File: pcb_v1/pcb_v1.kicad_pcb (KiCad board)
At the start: 2 copper layers, 8 parts, among them IC1 ESP32-WROOM-32UE-H4, IC2 DWM3000TR13, IC3 TC1017-3.3VLTTR, J1 Conn_02x03_Counter_Clockwise

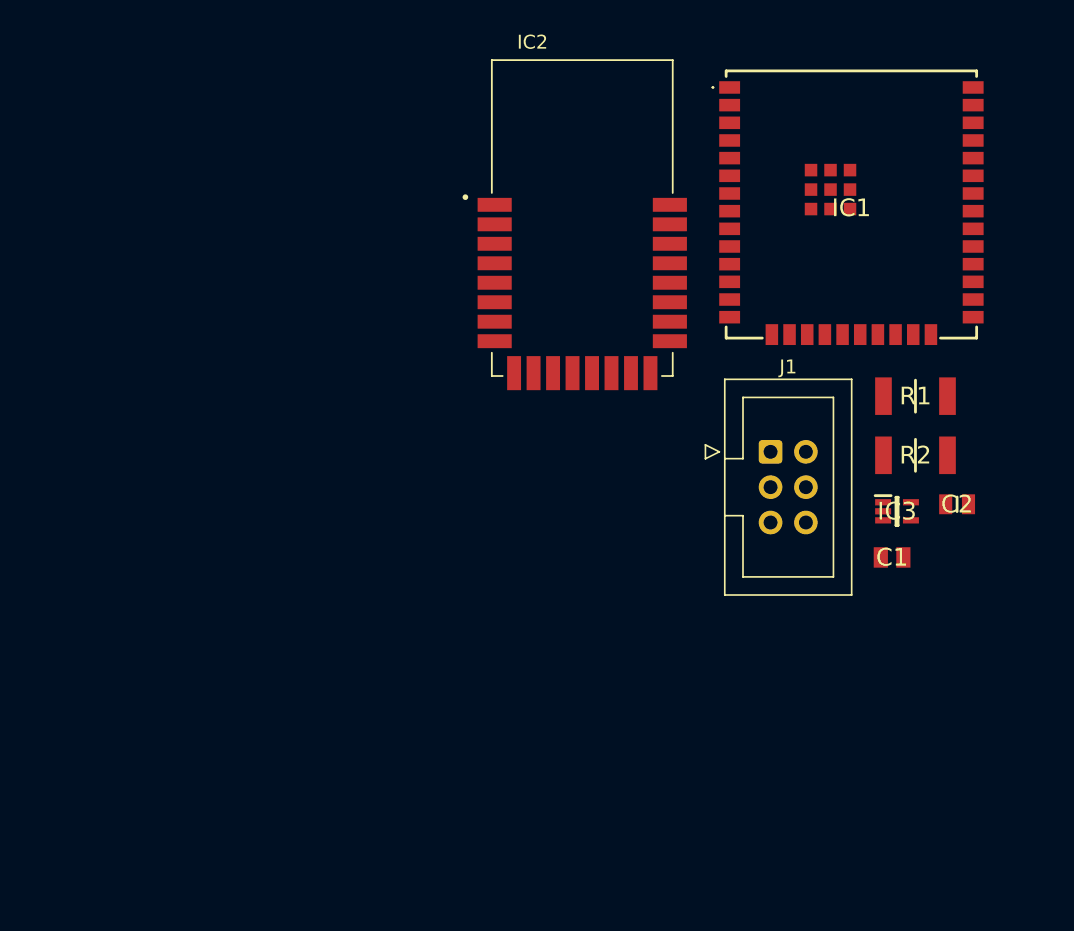
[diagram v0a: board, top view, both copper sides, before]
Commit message: pcb edits. add led footprints
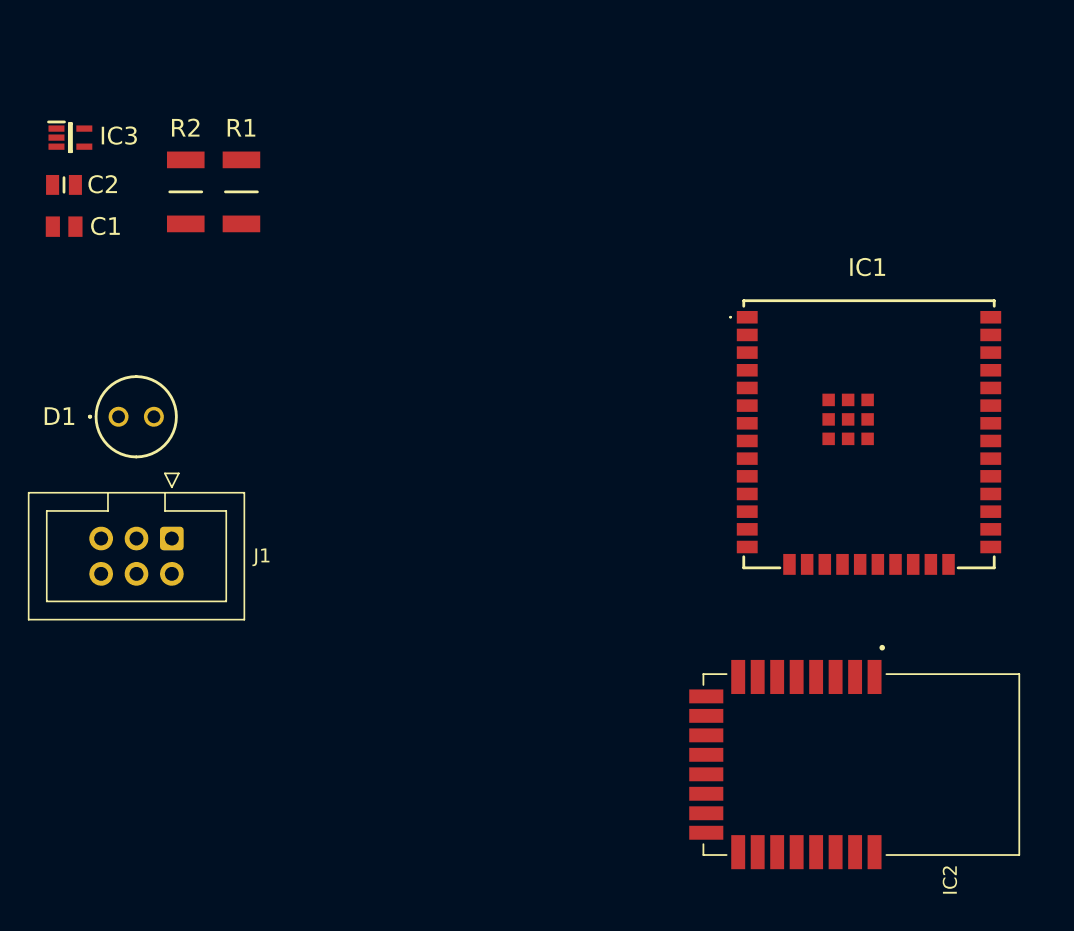
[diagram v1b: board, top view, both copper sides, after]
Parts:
- added D1: LED, led_footprint:QED123A4R0, F.Cu at (94.4, 99.0)
- moved C2 68.2 mm to (90.5, 82.3)
- moved IC3 65.2 mm to (91.0, 78.9)
- moved C1 64.1 mm to (90.5, 85.3), turned to 180 degrees
- moved R2 55.8 mm to (99.2, 82.8), turned to 90 degrees
- moved R1 50.6 mm to (103.2, 82.8), turned to 90 degrees
- moved IC2 44.1 mm to (147.8, 124.0), turned to -90 degrees
- moved J1 43.5 mm to (98.2, 107.7), turned to -90 degrees
- moved IC1 16.6 mm to (148.3, 100.2)

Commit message: update pin for jake baby
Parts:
- moved IC2 38.5 mm to (127.5, 91.2), turned to 0 degrees
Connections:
- IC2 pad 18: Net-(IC1-IO35) -> Net-(IC1-IO32)
- IC2 pad 19: Net-(IC1-IO32) -> Net-(IC1-IO35)
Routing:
- net Net-(IC1-IO25): track 0.00 -> 7.08 mm
- net Net-(IC1-IO35): track 0.00 -> 6.66 mm
- net Net-(IC1-IO32): track 0.00 -> 6.61 mm
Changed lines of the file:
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@@
   )
   (footprint "dwm3000_footprint:XCVR_DWM3000TR13" (layer "F.Cu")
-    (at 147.8 123.955 -90)
+    (at 127.545 91.2)
     (property "Height" "2.89")
     (property "Manufacturer_Name" "Qorvo")
@@
     (property "ki_description" "RF Modules DWM3000 UWB XCVR Module 23 x 13 x 2.9 mm")
     (attr smd)
-    (fp_text reference "IC2" (at 8.295 -6.4 90) (layer "F.SilkS")
+    (fp_text reference "IC2" (at 8.295 -6.4) (layer "F.SilkS")
         (effects (font (size 1 1) (thickness 0.15)))
     )
-    (fp_text value "DWM3000TR13" (at 3.41 13.865 90) (layer "F.Fab") hide
+    (fp_text value "DWM3000TR13" (at 3.41 13.865) (layer "F.Fab") hide
         (effects (font (size 1 1) (thickness 0.15)))
     )
@@
     (fp_circle (center -8.4 -1.5) (end -8.3 -1.5)
       (stroke (width 0.2) (type solid)) (fill none) (layer "F.Fab"))
-    (pad "1" smd rect (at -6.295 -0.95 270) (size 2.45 1) (layers "F.Cu" "F.Paste" "F.Mask")
+    (pad "1" smd rect (at -6.295 -0.95) (size 2.45 1) (layers "F.Cu" "F.Paste" "F.Mask")
       (net 37 "unconnected-(IC2-EXTON-Pad1)") (pinfunction "EXTON") (pintype "passive+no_connect") (solder_mask_margin 0.102))
-    (pad "2" smd rect (at -6.295 0.45 270) (size 2.45 1) (layers "F.Cu" "F.Paste" "F.Mask")
+    (pad "2" smd rect (at -6.295 0.45) (size 2.45 1) (layers "F.Cu" "F.Paste" "F.Mask")
       (net 38 "unconnected-(IC2-WAKEUP-Pad2)") (pinfunction "WAKEUP") (pintype "passive+no_connect") (solder_mask_margin 0.102))
-    (pad "3" smd rect (at -6.295 1.85 270) (size 2.45 1) (layers "F.Cu" "F.Paste" "F.Mask")
+    (pad "3" smd rect (at -6.295 1.85) (size 2.45 1) (layers "F.Cu" "F.Paste" "F.Mask")
       (net 11 "Net-(IC1-IO26)") (pinfunction "RSTN") (pintype "passive") (solder_mask_margin 0.102))
-    (pad "4" smd rect (at -6.295 3.25 270) (size 2.45 1) (layers "F.Cu" "F.Paste" "F.Mask")
+    (pad "4" smd rect (at -6.295 3.25) (size 2.45 1) (layers "F.Cu" "F.Paste" "F.Mask")
       (net 39 "unconnected-(IC2-GPIO7-Pad4)") (pinfunction "GPIO7") (pintype "passive+no_connect") (solder_mask_margin 0.102))
-    (pad "5" smd rect (at -6.295 4.65 270) (size 2.45 1) (layers "F.Cu" "F.Paste" "F.Mask")
+    (pad "5" smd rect (at -6.295 4.65) (size 2.45 1) (layers "F.Cu" "F.Paste" "F.Mask")
       (net 3 "VDD") (pinfunction "VDD1") (pintype "passive") (solder_mask_margin 0.102))
-    (pad "6" smd rect (at -6.295 6.05 270) (size 2.45 1) (layers "F.Cu" "F.Paste" "F.Mask")
+    (pad "6" smd rect (at -6.295 6.05) (size 2.45 1) (layers "F.Cu" "F.Paste" "F.Mask")
       (net 3 "VDD") (pinfunction "VDD3V3_1") (pintype "passive") (solder_mask_margin 0.102))
-    (pad "7" smd rect (at -6.295 7.45 270) (size 2.45 1) (layers "F.Cu" "F.Paste" "F.Mask")
+    (pad "7" smd rect (at -6.295 7.45) (size 2.45 1) (layers "F.Cu" "F.Paste" "F.Mask")
       (net 3 "VDD") (pinfunction "VDD3V3_2") (pintype "passive") (solder_mask_margin 0.102))
-    (pad "8" smd rect (at -6.295 8.85 270) (size 2.45 1) (layers "F.Cu" "F.Paste" "F.Mask")
+    (pad "8" smd rect (at -6.295 8.85) (size 2.45 1) (layers "F.Cu" "F.Paste" "F.Mask")
       (net 2 "GND") (pinfunction "VSS_1") (pintype "passive") (solder_mask_margin 0.102))
-    (pad "9" smd rect (at -4.9 11.145 270) (size 1 2.45) (layers "F.Cu" "F.Paste" "F.Mask")
+    (pad "9" smd rect (at -4.9 11.145) (size 1 2.45) (layers "F.Cu" "F.Paste" "F.Mask")
       (net 40 "unconnected-(IC2-GPIO6-Pad9)") (pinfunction "GPIO6") (pintype "passive+no_connect") (solder_mask_margin 0.102))
-    (pad "10" smd rect (at -3.5 11.145 270) (size 1 2.45) (layers "F.Cu" "F.Paste" "F.Mask")
+    (pad "10" smd rect (at -3.5 11.145) (size 1 2.45) (layers "F.Cu" "F.Paste" "F.Mask")
       (net 41 "unconnected-(IC2-GPIO5-Pad10)") (pinfunction "GPIO5") (pintype "passive+no_connect") (solder_mask_margin 0.102))
-    (pad "11" smd rect (at -2.1 11.145 270) (size 1 2.45) (layers "F.Cu" "F.Paste" "F.Mask")
+    (pad "11" smd rect (at -2.1 11.145) (size 1 2.45) (layers "F.Cu" "F.Paste" "F.Mask")
       (net 42 "unconnected-(IC2-GPIO4-Pad11)") (pinfunction "GPIO4") (pintype "passive+no_connect") (solder_mask_margin 0.102))
-    (pad "12" smd rect (at -0.7 11.145 270) (size 1 2.45) (layers "F.Cu" "F.Paste" "F.Mask")
+    (pad "12" smd rect (at -0.7 11.145) (size 1 2.45) (layers "F.Cu" "F.Paste" "F.Mask")
       (net 43 "Net-(IC2-GPIO3)") (pinfunction "GPIO3") (pintype "passive") (solder_mask_margin 0.102))
-    (pad "13" smd rect (at 0.7 11.145 270) (size 1 2.45) (layers "F.Cu" "F.Paste" "F.Mask")
+    (pad "13" smd rect (at 0.7 11.145) (size 1 2.45) (layers "F.Cu" "F.Paste" "F.Mask")
       (net 44 "unconnected-(IC2-GPIO2-Pad13)") (pinfunction "GPIO2") (pintype "passive+no_connect") (solder_mask_margin 0.102))
-    (pad "14" smd rect (at 2.1 11.145 270) (size 1 2.45) (layers "F.Cu" "F.Paste" "F.Mask")
+    (pad "14" smd rect (at 2.1 11.145) (size 1 2.45) (layers "F.Cu" "F.Paste" "F.Mask")
       (net 45 "unconnected-(IC2-GPIO1-Pad14)") (pinfunction "GPIO1") (pintype "passive+no_connect") (solder_mask_margin 0.102))
-    (pad "15" smd rect (at 3.5 11.145 270) (size 1 2.45) (layers "F.Cu" "F.Paste" "F.Mask")
+    (pad "15" smd rect (at 3.5 11.145) (size 1 2.45) (layers "F.Cu" "F.Paste" "F.Mask")
       (net 46 "unconnected-(IC2-GPIO0-Pad15)") (pinfunction "GPIO0") (pintype "passive+no_connect") (solder_mask_margin 0.102))
-    (pad "16" smd rect (at 4.9 11.145 270) (size 1 2.45) (layers "F.Cu" "F.Paste" "F.Mask")
+    (pad "16" smd rect (at 4.9 11.145) (size 1 2.45) (layers "F.Cu" "F.Paste" "F.Mask")
       (net 2 "GND") (pinfunction "VSS_2") (pintype "passive") (solder_mask_margin 0.102))
-    (pad "17" smd rect (at 6.295 8.85 270) (size 2.45 1) (layers "F.Cu" "F.Paste" "F.Mask")
+    (pad "17" smd rect (at 6.295 8.85) (size 2.45 1) (layers "F.Cu" "F.Paste" "F.Mask")
       (net 10 "Net-(IC1-IO25)") (pinfunction "SPICSN") (pintype "passive") (solder_mask_margin 0.102))
-    (pad "18" smd rect (at 6.295 7.45 270) (size 2.45 1) (layers "F.Cu" "F.Paste" "F.Mask")
-      (net 7 "Net-(IC1-IO35)") (pinfunction "SPIMOSI") (pintype "passive") (solder_mask_margin 0.102))
-    (pad "19" smd rect (at 6.295 6.05 270) (size 2.45 1) (layers "F.Cu" "F.Paste" "F.Mask")
-      (net 8 "Net-(IC1-IO32)") (pinfunction "SPIMISO") (pintype "passive") (solder_mask_margin 0.102))
-    (pad "20" smd rect (at 6.295 4.65 270) (size 2.45 1) (layers "F.Cu" "F.Paste" "F.Mask")
+    (pad "18" smd rect (at 6.295 7.45) (size 2.45 1) (layers "F.Cu" "F.Paste" "F.Mask")
+      (net 8 "Net-(IC1-IO32)") (pinfunction "SPIMOSI") (pintype "passive") (solder_mask_margin 0.102))
+    (pad "19" smd rect (at 6.295 6.05) (size 2.45 1) (layers "F.Cu" "F.Paste" "F.Mask")
+      (net 7 "Net-(IC1-IO35)") (pinfunction "SPIMISO") (pintype "passive") (solder_mask_margin 0.102))
+    (pad "20" smd rect (at 6.295 4.65) (size 2.45 1) (layers "F.Cu" "F.Paste" "F.Mask")
       (net 9 "Net-(IC1-IO33)") (pinfunction "SPICLK") (pintype "passive") (solder_mask_margin 0.102))
-    (pad "21" smd rect (at 6.295 3.25 270) (size 2.45 1) (layers "F.Cu" "F.Paste" "F.Mask")
+    (pad "21" smd rect (at 6.295 3.25) (size 2.45 1) (layers "F.Cu" "F.Paste" "F.Mask")
       (net 2 "GND") (pinfunction "VSS_3") (pintype "passive") (solder_mask_margin 0.102))
-    (pad "22" smd rect (at 6.295 1.85 270) (size 2.45 1) (layers "F.Cu" "F.Paste" "F.Mask")
+    (pad "22" smd rect (at 6.295 1.85) (size 2.45 1) (layers "F.Cu" "F.Paste" "F.Mask")
       (net 47 "Net-(IC2-GPIO8)") (pinfunction "GPIO8") (pintype "passive") (solder_mask_margin 0.102))
-    (pad "23" smd rect (at 6.295 0.45 270) (size 2.45 1) (layers "F.Cu" "F.Paste" "F.Mask")
+    (pad "23" smd rect (at 6.295 0.45) (size 2.45 1) (layers "F.Cu" "F.Paste" "F.Mask")
       (net 2 "GND") (pinfunction "VSS_4") (pintype "passive") (solder_mask_margin 0.102))
-    (pad "24" smd rect (at 6.295 -0.95 270) (size 2.45 1) (layers "F.Cu" "F.Paste" "F.Mask")
+    (pad "24" smd rect (at 6.295 -0.95) (size 2.45 1) (layers "F.Cu" "F.Paste" "F.Mask")
       (net 2 "GND") (pinfunction "VSS_5") (pintype "passive") (solder_mask_margin 0.102))
     (zone (net 0) (net_name "") (layer "F.Cu") (hatch full 0.508)
@@
       (polygon
         (pts
-          (xy 159.15 117.455)
-          (xy 159.15 130.455)
-          (xy 149.375 130.455)
-          (xy 149.375 117.455)
+          (xy 121.045 79.85)
+          (xy 134.045 79.85)
+          (xy 134.045 89.625)
+          (xy 121.045 89.625)
         )
       )
@@
       (polygon
         (pts
-          (xy 159.15 117.455)
-          (xy 159.15 130.455)
-          (xy 149.375 130.455)
-          (xy 149.375 117.455)
+          (xy 121.045 79.85)
+          (xy 134.045 79.85)
+          (xy 134.045 89.625)
+          (xy 121.045 89.625)
         )
       )
@@
       (polygon
         (pts
-          (xy 159.15 117.455)
-          (xy 159.15 130.455)
-          (xy 149.375 130.455)
-          (xy 149.375 117.455)
+          (xy 121.045 79.85)
+          (xy 134.045 79.85)
+          (xy 134.045 89.625)
+          (xy 121.045 89.625)
         )
       )
@@
     )
   )
+  (segment (start 139.02 99.43) (end 139.6 99.43) (width 0.25) (layer "F.Cu") (net 7))
+  (segment (start 133.84 97.25) (end 136.84 97.25) (width 0.25) (layer "F.Cu") (net 7))
+  (segment (start 136.84 97.25) (end 139.02 99.43) (width 0.25) (layer "F.Cu") (net 7))
+  (segment (start 133.84 98.65) (end 135.315 98.65) (width 0.25) (layer "F.Cu") (net 8))
+  (segment (start 135.315 98.65) (end 137.365 100.7) (width 0.25) (layer "F.Cu") (net 8))
+  (segment (start 137.365 100.7) (end 139.6 100.7) (width 0.25) (layer "F.Cu") (net 8))
+  (segment (start 137.03 103.24) (end 139.6 103.24) (width 0.25) (layer "F.Cu") (net 10))
+  (segment (start 133.84 100.05) (end 137.03 103.24) (width 0.25) (layer "F.Cu") (net 10))
 )

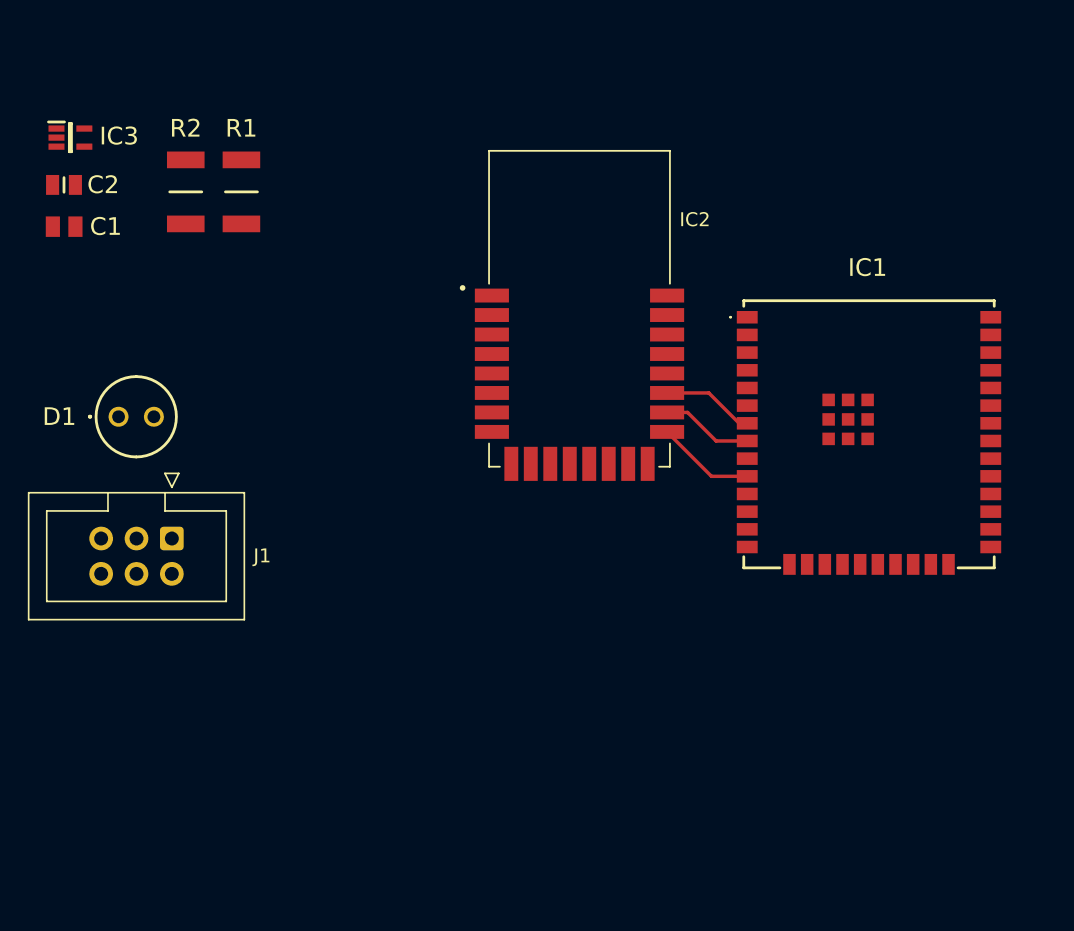
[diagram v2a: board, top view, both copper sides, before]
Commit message: files for esp32 development. added li poly charger connector to schematic build.
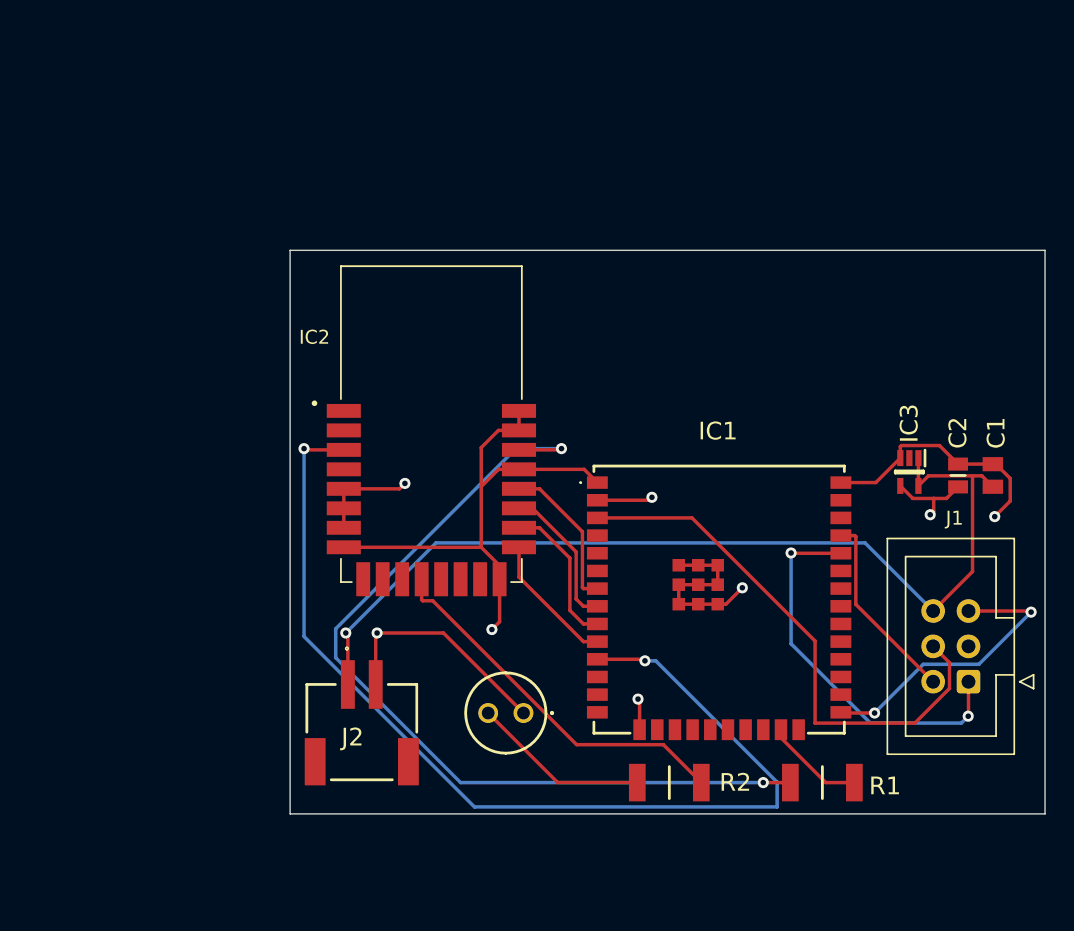
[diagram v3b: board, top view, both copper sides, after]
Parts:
- added J2: 1769, lipo_charger_footprint:1769, F.Cu at (111.9, 118.2)
- moved C1 69.1 mm to (157.2, 103.2), turned to 90 degrees
- moved C2 67.6 mm to (154.8, 103.2), turned to 90 degrees
- moved IC3 64.9 mm to (151.2, 102.9), turned to -90 degrees
- moved R1 59.5 mm to (145.0, 125.2), turned to 0 degrees
- moved J1 58.2 mm to (155.5, 118.0), turned to 180 degrees
- moved R2 54.9 mm to (134.0, 125.2), turned to 180 degrees
- moved D1 36.1 mm to (123.5, 120.2), turned to 0 degrees
- moved IC1 16.0 mm to (137.6, 112.1)
- moved IC2 13.5 mm to (116.9, 99.5)
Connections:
- IC1 pad 23: unconnected-(IC1-IO15-Pad23) -> Net-(IC1-IO15)
- IC1 pad 24: Net-(IC1-IO2) -> unconnected-(IC1-IO2-Pad24)
- IC1 pad 6: GND -> unconnected-(IC1-IO34-Pad6)
- IC2 pad 18: Net-(IC1-IO32) -> Net-(IC1-IO33)
- IC2 pad 19: Net-(IC1-IO35) -> Net-(IC1-IO32)
- IC2 pad 20: Net-(IC1-IO33) -> Net-(IC1-IO35)
- J1 pad 1: Net-(IC1-TXD0) -> Net-(IC1-RXD0)
- J1 pad 2: Net-(IC1-RXD0) -> Net-(IC1-TXD0)
- J1 pad 4: Net-(IC3-VIN) -> Net-(IC1-EN)
- J1 pad 6: Net-(IC1-EN) -> Net-(IC3-VIN)
- R1 pad 2: Net-(IC1-IO2) -> Net-(IC1-IO15)
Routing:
- net GND: track 0.00 -> 157.1 mm, vias 0 -> 5
- net Net-(IC1-IO26): track 0.00 -> 73.8 mm, vias 0 -> 2
- net Net-(IC3-VIN): track 0.00 -> 69.5 mm, vias 0 -> 1
- net Net-(IC2-GPIO8): track 0.00 -> 63.1 mm, vias 0 -> 2
- net VDD: track 0.00 -> 56.2 mm, vias 0 -> 3
- net Net-(IC1-EN): track 0.00 -> 39.4 mm
- net Net-(IC1-RXD0): track 0.00 -> 27.9 mm, vias 0 -> 2
- net Net-(IC2-GPIO3): track 0.00 -> 27.0 mm
- net Net-(IC1-IO0): track 0.00 -> 21.2 mm, vias 0 -> 2
- net Net-(IC1-TXD0): track 0.00 -> 13.8 mm
- net Net-(D1-A): track 0.00 -> 12.8 mm
- net Net-(IC1-IO33): track 0.00 -> 10.7 mm
- net Net-(IC1-IO15): track 0.00 -> 7.19 mm
- net Net-(IC1-IO35): track 6.66 -> 11.0 mm
- net Net-(IC1-IO32): track 6.61 -> 10.5 mm
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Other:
- board outline added: 54.2 x 40.5 mm
- copper layers 2 -> 4
- board text added: "SDP TEAM 8 SWAN v1"
